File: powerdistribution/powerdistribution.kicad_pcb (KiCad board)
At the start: 4 copper layers, 105 x 75 mm, 123 parts, among them J1 282837-2, J2 282837-2, J3 ESQ-113-12-G-D, J6 Conn_01x02, M1 Motor_Servo, M2 Motor_Servo, Q1 IRLML0030, Q2 IRLML0030, Q3 IRLML0030, Q5 IRLML0030, U1 BQ7790512PW, U10 TPS1HC30BQPWPRQ1, U3 AP64501QSP-13, U4 AP64501QSP-13, U5 TPS1HC30BQPWPRQ1, U6 TPS1HC30BQPWPRQ1, U9 MIC29302AWD-TR

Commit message: starting new placement
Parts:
- added C42: 1uF, Capacitor_SMD:C_0603_1608Metric_Pad1.08x0.95mm_HandSolder, F.Cu at (105.2, 41.7)
- added C43: 1uF, Capacitor_SMD:C_0603_1608Metric_Pad1.08x0.95mm_HandSolder, F.Cu at (105.2, 44.2)
- added IC1: NCP718ASNADJT1G, HPRfootprints:NCP718_SOT95P280X100-5N, F.Cu at (110.0, 42.7)
- added R54: 19k, Resistor_SMD:R_0603_1608Metric_Pad0.98x0.95mm_HandSolder, F.Cu at (105.2, 46.7)
- added R55: 6k, Resistor_SMD:R_0603_1608Metric_Pad0.98x0.95mm_HandSolder, F.Cu at (105.2, 49.2)
- moved R51 135.2 mm to (-37.8, 130.8), turned to 90 degrees
- moved R50 135.2 mm to (-37.8, 127.0), turned to 90 degrees
- moved R33 132.4 mm to (-33.0, 137.0), turned to 0 degrees
- moved R30 131.4 mm to (-33.0, 133.8), turned to 0 degrees
- moved R32 130.8 mm to (-33.0, 130.8), turned to 180 degrees
- moved C35 128.4 mm to (-27.8, 140.0), turned to 0 degrees
- moved TP4 127.4 mm to (-37.0, 139.2), turned to 0 degrees
- moved R29 126.6 mm to (-34.8, 127.0), turned to -90 degrees
- moved R34 123.2 mm to (-27.8, 137.0), turned to 0 degrees
- moved TP2 121.2 mm to (-37.0, 122.5), turned to 0 degrees
- moved R27 118.1 mm to (-35.7, 81.5)
- moved C32 118.1 mm to (-19.1, 75.8)
- moved C33 118.1 mm to (-35.4, 84.5)
- moved C40 118.1 mm to (-12.9, 69.5)
- moved R21 118.1 mm to (-26.5, 71.0)
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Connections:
- J3 pad 01: GND -> unconnected-(J3-Pad01)
- J3 pad 02: Net-(J3-Pad02) -> unconnected-(J3-Pad02)
- J3 pad 03: GND -> unconnected-(J3-Pad03)
- J3 pad 04: Net-(J3-Pad04) -> unconnected-(J3-Pad04)
- J3 pad 05: GND -> unconnected-(J3-Pad05)
- J3 pad 06: /aux7_rx -> unconnected-(J3-Pad06)
- J3 pad 07: GND -> unconnected-(J3-Pad07)
- J3 pad 08: /aux7_tx -> unconnected-(J3-Pad08)
- J3 pad 09: GND -> unconnected-(J3-Pad09)
- J3 pad 10: /can_rx -> unconnected-(J3-Pad10)
- J3 pad 11: GND -> unconnected-(J3-Pad11)
- J3 pad 12: /can_tx -> unconnected-(J3-Pad12)
- J3 pad 13: /5V -> unconnected-(J3-Pad13)
- J3 pad 14: /SENSE_mosi -> unconnected-(J3-Pad14)
- J3 pad 15: /5V -> unconnected-(J3-Pad15)
- J3 pad 16: /SENSE_miso -> unconnected-(J3-Pad16)
- J3 pad 17: /5V -> unconnected-(J3-Pad17)
- J3 pad 18: /SENSE_sck -> unconnected-(J3-Pad18)
- J3 pad 19: /5V -> unconnected-(J3-Pad19)
- J3 pad 20: /servo2_pwm -> unconnected-(J3-Pad20)
- J3 pad 21: /5V -> unconnected-(J3-Pad21)
- J3 pad 22: /servo1_pwm -> unconnected-(J3-Pad22)
- J3 pad 23: /5V -> unconnected-(J3-Pad23)
- J3 pad 24: /PYRO1 -> unconnected-(J3-Pad24)
- J3 pad 26: /PYRO2 -> unconnected-(J3-Pad26)
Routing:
- net Net-(BT1-Pad1+): track 119.4 -> 0.00 mm
- net Net-(BT1-Pad2+): track 106.4 -> 0.00 mm
- net /6V: track 70.2 -> 0.00 mm
- net /LDO_5V: track 64.9 -> 0.00 mm, vias 6 -> 0
- net /5V: track 62.5 -> 0.00 mm
- net Net-(U4-EN): track 39.4 -> 0.00 mm
- net Net-(U10-VOUT): track 34.0 -> 0.00 mm
- net Net-(U5-VOUT): track 33.5 -> 0.00 mm
- net GND: track 30.8 -> 0.00 mm, vias 62 -> 0
- net /6V_EN: track 29.5 -> 0.00 mm
- net /PYRO1: track 28.8 -> 0.00 mm, vias 1 -> 0
- net Net-(Q5-D): track 28.2 -> 0.00 mm
- net /servo2_pwm: track 24.1 -> 0.00 mm
- net /6V_DIAGEN: track 23.7 -> 0.00 mm
- net Net-(U1-TS): track 19.4 -> 0.00 mm
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- removed copper zone on In2.Cu, net /Pack+
- removed copper zone on In1.Cu, net GND

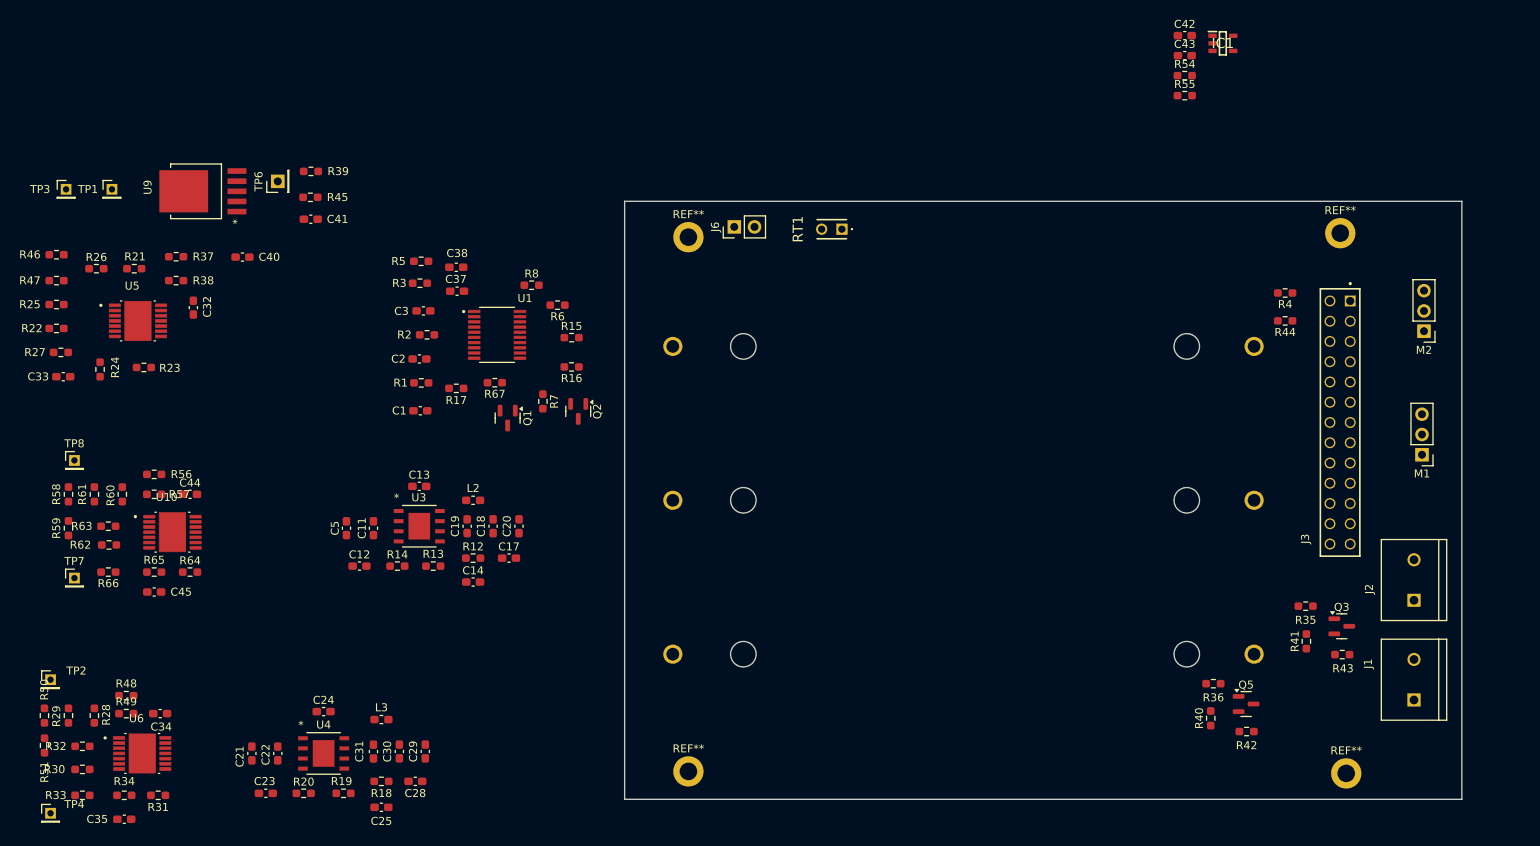
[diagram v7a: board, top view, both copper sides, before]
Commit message: power board placed and routed except connector, increased board length by 5mm
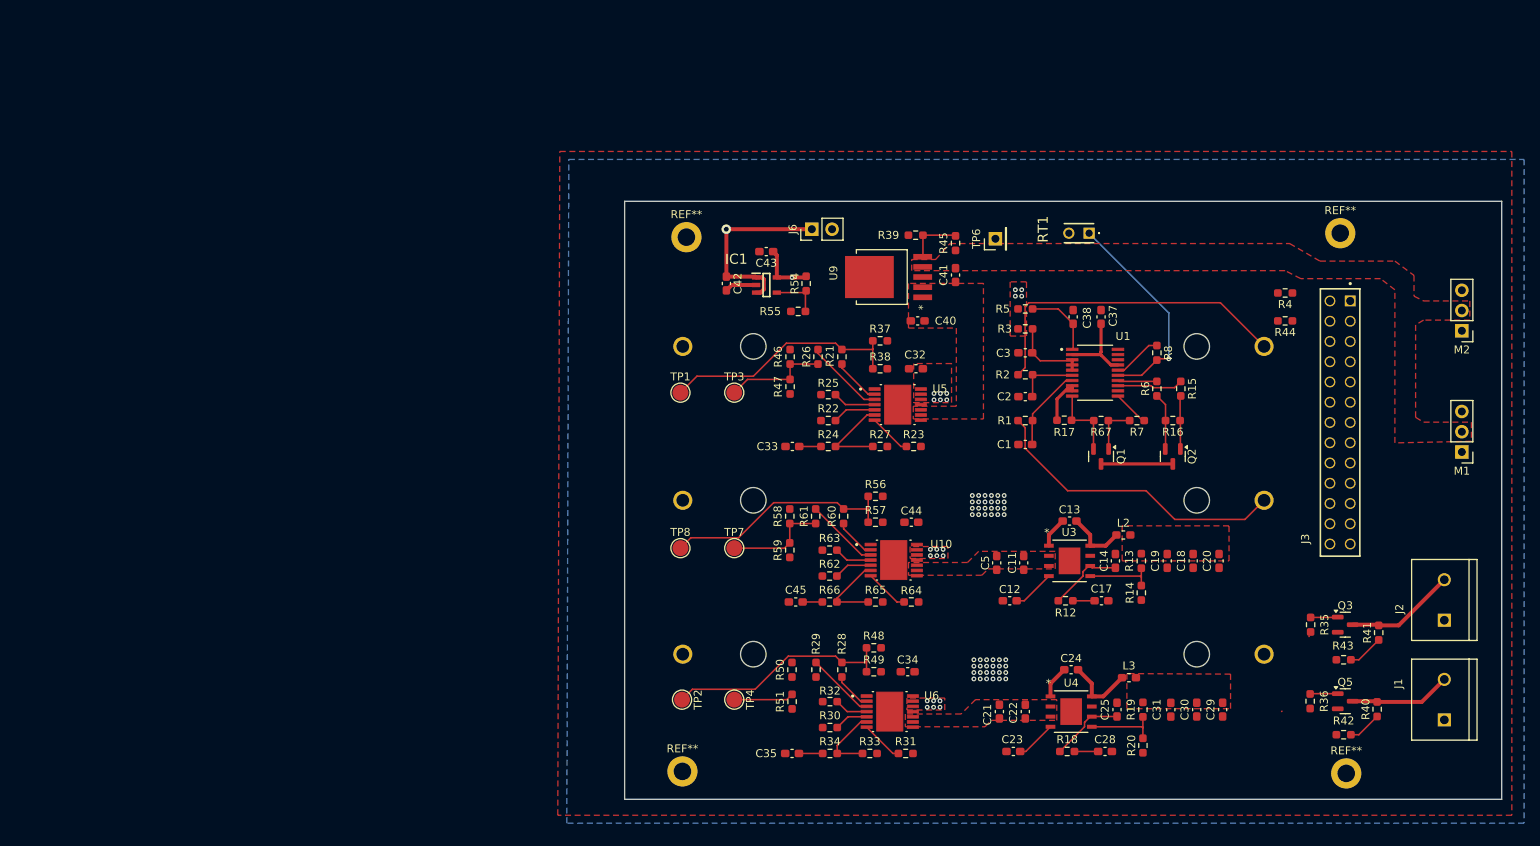
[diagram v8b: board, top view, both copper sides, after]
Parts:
- TP1, TP2, TP3, TP4, TP7, TP8: footprint Connector_PinHeader_2.00mm:PinHeader_1x01_P2.00mm_Vertical -> TestPoint:TestPoint_Pad_D2.0mm
- moved R20 105.4 mm to (100.0, 130.8), turned to 90 degrees
- moved R27 103.4 mm to (67.0, 93.2), turned to 180 degrees
- moved R19 100.8 mm to (100.0, 126.2), turned to -90 degrees
- moved C29 100.1 mm to (110.0, 126.2)
- moved C30 100.1 mm to (106.8, 126.2)
- moved C31 100.1 mm to (103.5, 126.3)
- moved R33 98.9 mm to (65.8, 131.8), turned to 180 degrees
- moved R22 97.5 mm to (60.5, 90.0)
- moved R25 97.4 mm to (60.5, 86.8)
- moved R23 97.0 mm to (71.2, 93.2)
- moved U5 95.9 mm to (69.2, 88.0)
- moved R48 93.9 mm to (66.2, 118.5), turned to 0 degrees
- moved R28 93.9 mm to (62.2, 121.2)
- moved R29 93.9 mm to (59.0, 121.2), turned to 90 degrees
- moved R50 93.9 mm to (56.0, 121.2)
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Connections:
- net Net-(BT1-Pad1+) renamed /B1
- net Net-(BT1-Pad2+) renamed /B2
- net Net-(U10-VOUT) renamed /XV_SWout
- net Net-(U4-EN) renamed /5V_SWout
- net Net-(U5-VOUT) renamed /6V_SWout
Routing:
- net /B2: track 0.00 -> 41.4 mm
- net /B1: track 0.00 -> 38.5 mm
- net /6V_EN: track 0.00 -> 30.6 mm
- net /12V_EN: track 0.00 -> 29.5 mm
- net /5V_EN: track 0.00 -> 28.8 mm
- net Net-(U1-TS): track 0.00 -> 27.1 mm, vias 0 -> 1
- net /Pack+: track 0.00 -> 23.9 mm, vias 0 -> 23
- net Net-(Q3-D): track 0.00 -> 13.9 mm
- net /6V_DIAGEN: track 0.00 -> 13.1 mm
- net /12V_DIAGEN: track 0.00 -> 12.9 mm
- net Net-(Q5-D): track 0.00 -> 12.7 mm
- net Net-(U5-SNS): track 0.00 -> 11.2 mm
- net Net-(U1-VC1): track 0.00 -> 10.6 mm
- net Net-(U10-SNS): track 0.00 -> 10.5 mm
- net Net-(U1-AVDD): track 0.00 -> 10.2 mm
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- added copper zone on F.Cu, net /12V
- added copper zone on F.Cu, net /5V_SWout
- added copper zone on F.Cu, net /6V
- added copper zone on F.Cu, net /6V_SWout
- added copper zone on In2.Cu, net /B1
- added copper zone on In2.Cu, net /B2
- added copper zone on F.Cu, net /Pack+
- added copper zone on In2.Cu, net /Pack+
- added copper zone on F.Cu, net /XV_SWout
- added copper zone on B.Cu, net GND
- added copper zone on F.Cu, net GND
- added copper zone on In1.Cu, net GND
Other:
- board size 105 x 75 mm -> 110 x 75 mm
- board text added: "${REFERENCE}"
